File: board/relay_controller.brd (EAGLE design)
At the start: 75 x 50 mm, 71 parts, among them IC1 STM32F103C8T, IC3 AT24C, X1 RJ45-8L21-S, X2 RJ45-8L21-S

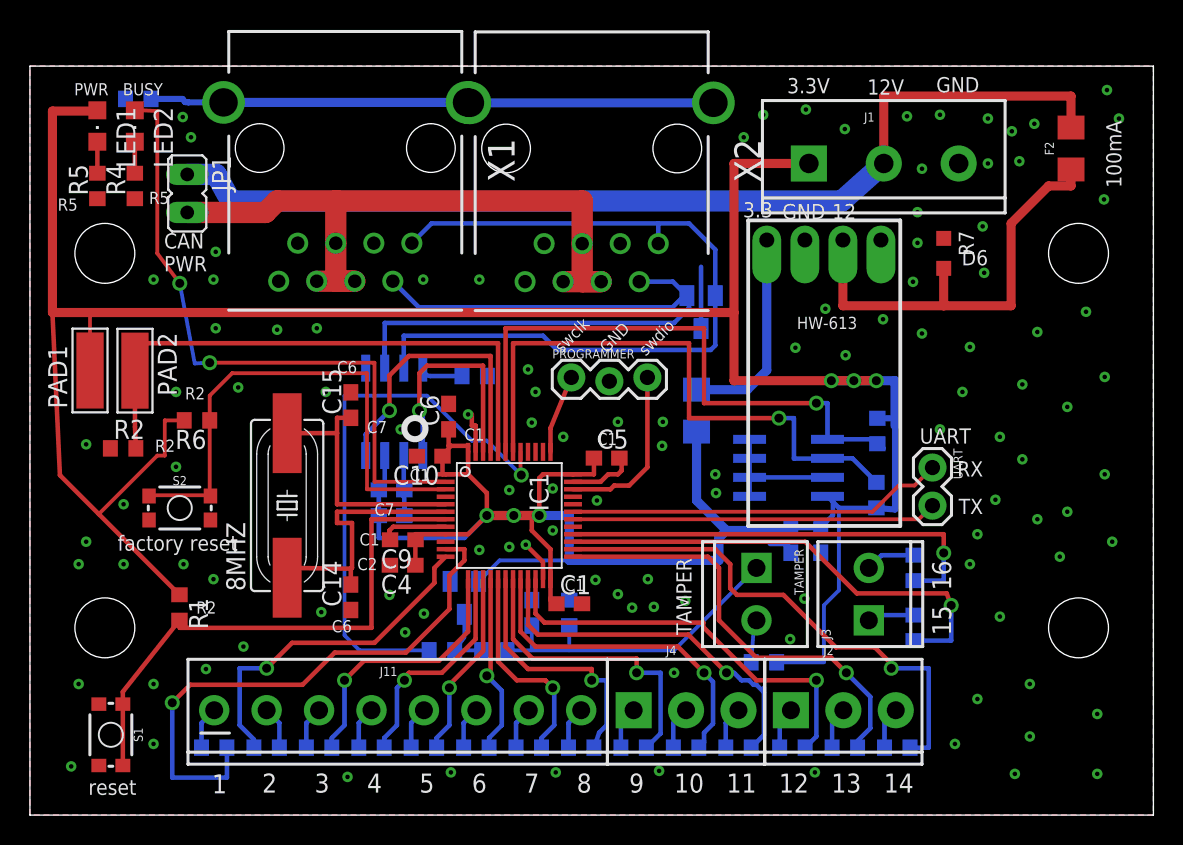
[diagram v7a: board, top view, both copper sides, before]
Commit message: jumpers for boot mode
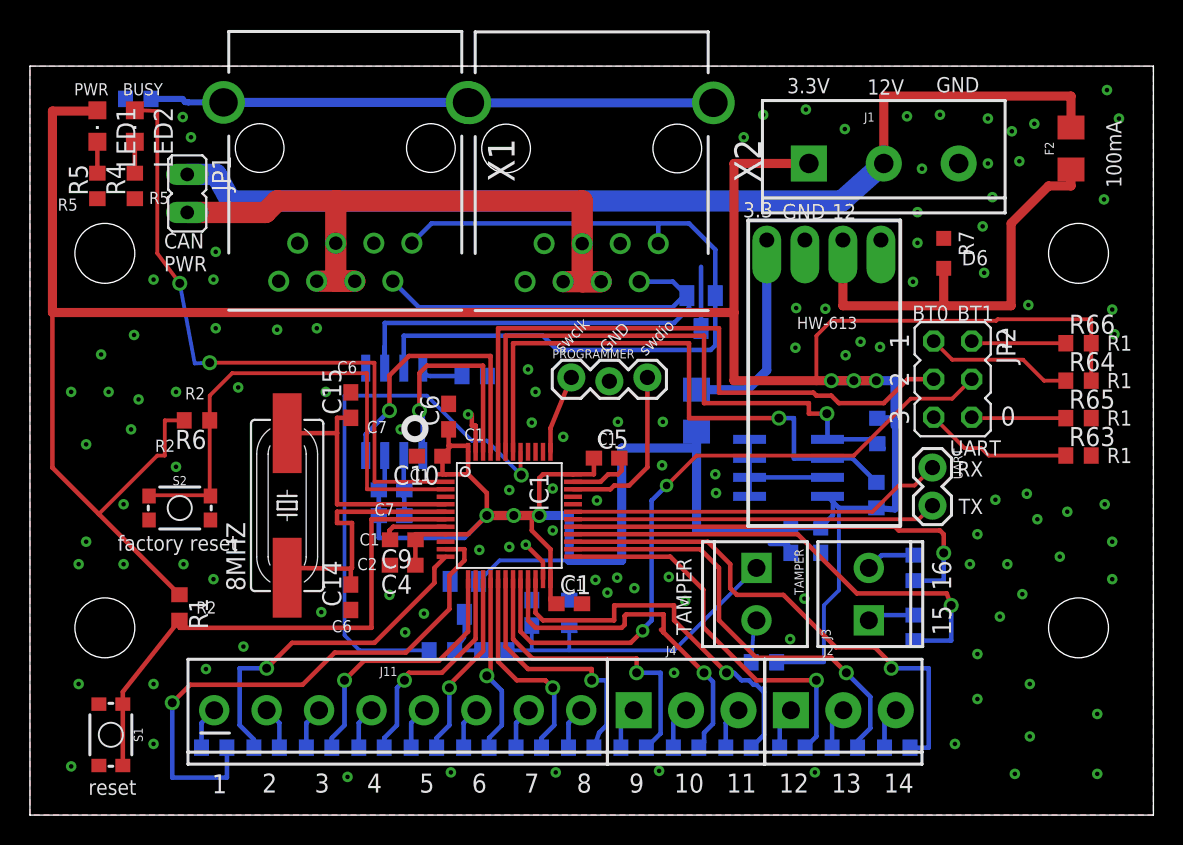
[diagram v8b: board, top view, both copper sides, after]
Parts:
- removed PAD1, PAD2: WIREPADSMD5-1,8, wirepad:5-1,8
- removed R2: 10k, rcl:R0603
- added JP2: (no value), jumper:JP3Q
- added R63, R64, R65, R66: 10k, rcl:R0603
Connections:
- removed net N$12: IC1.44, PAD2.1, R2.2
- new net BOOT0: IC1.44, JP2.3
- new net BOOT1: IC1.20, JP2.4
- new net N$29: JP2.2, R66.1
- new net N$30: JP2.1, R64.1
- new net N$31: JP2.6, R65.1
- new net N$32: JP2.5, R63.1
- net +3V3: now also R64.2, R66.2; no longer PAD1.1
- net GND: now also R63.2, R65.2; no longer R2.1
- net RELAY_10: now also IC1.21; no longer IC1.20
- net RELAY_11: now also IC1.22; no longer IC1.21
- net RELAY_12: now also IC1.25; no longer IC1.22
- net RELAY_13: now also IC1.26; no longer IC1.25
- net RELAY_14: now also IC1.27; no longer IC1.26
- net RELAY_15: now also IC1.28; no longer IC1.27
- net RELAY_16: now also IC1.29; no longer IC1.28
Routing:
- net BOOT1: track 0.00 -> 46.0 mm, vias 0 -> 2
- net BOOT0: track 0.00 -> 42.6 mm
- net N$12: track 39.2 -> 0.00 mm
- net +3V3: track 259.0 -> 285.2 mm
- net N$30: track 0.00 -> 9.91 mm
- net N$32: track 0.00 -> 9.88 mm
- net N$29: track 0.00 -> 6.34 mm
- net N$31: track 0.00 -> 6.30 mm
- net RELAY_12: track 27.9 -> 25.9 mm
- net RELAY_10: track 22.5 -> 23.6 mm
- net I2C1_SDA: track 41.2 -> 40.1 mm
- net RELAY_11: track 25.0 -> 26.0 mm
- net GND: vias 114 -> 118
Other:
- board text added: "0"
- board text added: "BT0"
- board text added: "BT1"
- board text added: "relay controller 2020.07.18 v1.1"
- board text removed: "relay controller 2020.07.13 v1.1"
